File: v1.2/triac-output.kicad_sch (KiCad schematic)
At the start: 7 parts, among them Q5 T835-600B, Q6 2N7002, U7 TLP160G

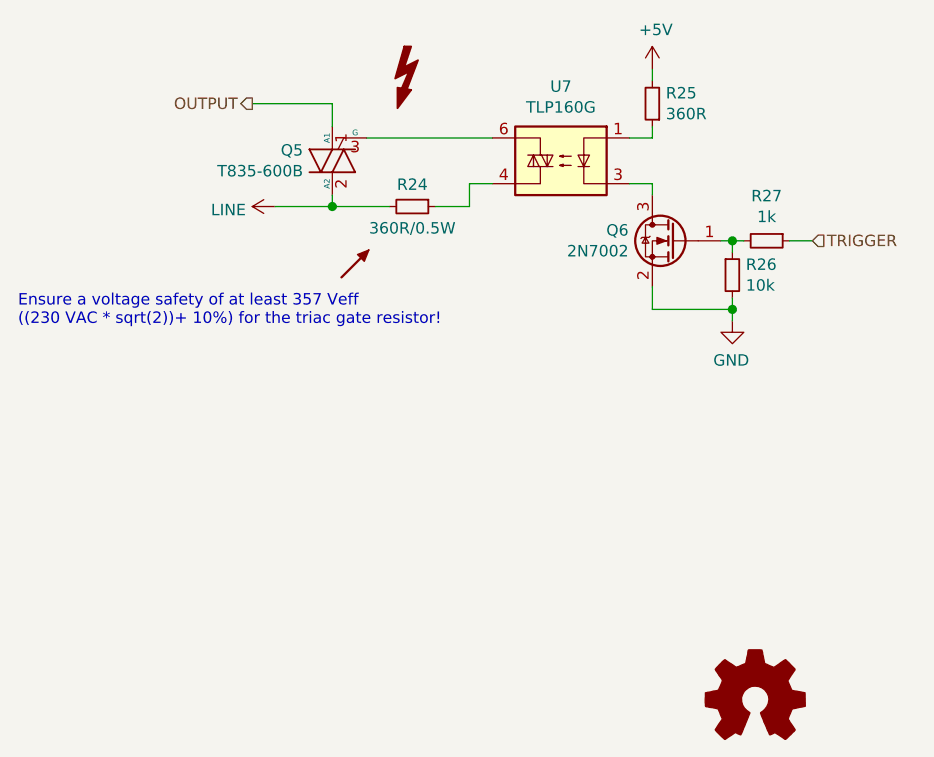
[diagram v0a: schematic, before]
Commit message: More updates
* make pump triac switch NEUT, not LINE
* move ADC a bit
* improve clearance
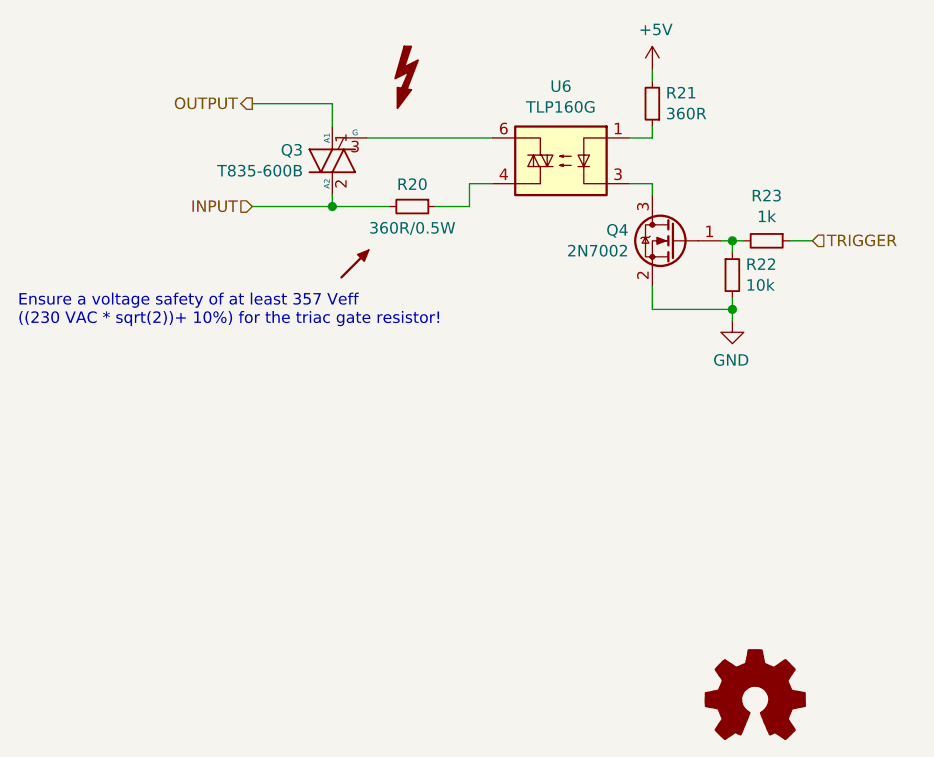
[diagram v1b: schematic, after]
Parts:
- renumbered Q5 to Q3, Q6 to Q4, R24 to R20, R25 to R21, R26 to R22, R27 to R23, U7 to U6
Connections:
- net LINE renamed INPUT
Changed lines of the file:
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@@
 (kicad_sch (version 20201015) (generator eeschema)
-  (page 0 6)
   (paper "A5")
   (title_block
@@
   (junction (at 133.35 60.96) (diameter 1.016) (color 0 0 0 0))
   (junction (at 133.35 68.58) (diameter 1.016) (color 0 0 0 0))
+  (wire (pts (xy 80.01 57.15) (xy 88.9 57.15))
+    (stroke (width 0) (type solid) (color 0 0 0 0))
+  )
   (wire (pts (xy 88.9 45.72) (xy 80.01 45.72))
     (stroke (width 0) (type solid) (color 0 0 0 0))
   )
   (wire (pts (xy 88.9 45.72) (xy 88.9 48.26))
-    (stroke (width 0) (type solid) (color 0 0 0 0))
-  )
-  (wire (pts (xy 88.9 57.15) (xy 82.55 57.15))
     (stroke (width 0) (type solid) (color 0 0 0 0))
   )
@@
     (effects (font (size 1.27 1.27)) (justify right))
   )
+  (hierarchical_label "INPUT" (shape input) (at 80.01 57.15 180)
+    (effects (font (size 1.27 1.27)) (justify right))
+  )
   (hierarchical_label "TRIGGER" (shape input) (at 142.24 60.96 0)
     (effects (font (size 1.27 1.27)) (justify left))
   )
-  (symbol (lib_id "power:LINE") (at 82.55 57.15 90) (mirror x)
-    (in_bom yes) (on_board yes)
-    (property "Reference" "#PWR048" (id 0) (at 86.36 57.15 0)
-      (effects (font (size 1.27 1.27)) hide)
-    )
-    (property "Value" "LINE" (id 1) (at 79.2988 57.531 90)
-      (effects (font (size 1.27 1.27)) (justify left))
-    )
-    (property "Footprint" "" (id 2) (at 82.55 57.15 0)
-      (effects (font (size 1.27 1.27)) hide)
-    )
-    (property "Datasheet" "" (id 3) (at 82.55 57.15 0)
-      (effects (font (size 1.27 1.27)) hide)
-    )
-  )
   (symbol (lib_id "power:+5V") (at 124.46 41.91 0)
     (in_bom yes) (on_board yes)
@@
   (symbol (lib_id "Device:R_Small") (at 97.79 57.15 270)
     (in_bom yes) (on_board yes)
-    (property "Reference" "R24" (id 0) (at 97.79 54.7116 90))
+    (property "Reference" "R20" (id 0) (at 97.79 54.7116 90))
     (property "Value" "360R/0.5W" (id 1) (at 97.79 59.563 90))
     (property "Footprint" "Resistor_SMD:R_1206_3216Metric_Pad1.30x1.75mm_HandSolder" (id 2) (at 97.79 57.15 0)
@@
   (symbol (lib_id "Device:R_Small") (at 124.46 45.72 180)
     (in_bom yes) (on_board yes)
-    (property "Reference" "R25" (id 0) (at 125.9586 44.5516 0)
+    (property "Reference" "R21" (id 0) (at 125.9586 44.5516 0)
       (effects (font (size 1.27 1.27)) (justify right))
     )
@@
   (symbol (lib_id "Device:R_Small") (at 133.35 64.77 0)
     (in_bom yes) (on_board yes)
-    (property "Reference" "R26" (id 0) (at 134.8486 63.6016 0)
+    (property "Reference" "R22" (id 0) (at 134.8486 63.6016 0)
       (effects (font (size 1.27 1.27)) (justify left))
     )
@@
   (symbol (lib_id "Device:R_Small") (at 137.16 60.96 270)
     (in_bom yes) (on_board yes)
-    (property "Reference" "R27" (id 0) (at 137.16 55.9816 90))
+    (property "Reference" "R23" (id 0) (at 137.16 55.9816 90))
     (property "Value" "1k" (id 1) (at 137.16 58.293 90))
     (property "Footprint" "Resistor_SMD:R_0603_1608Metric_Pad0.98x0.95mm_HandSolder" (id 2) (at 137.16 60.96 0)
@@
   (symbol (lib_id "Triac_Thyristor:BT138-600") (at 88.9 52.07 180)
     (in_bom yes) (on_board yes)
-    (property "Reference" "Q5" (id 0) (at 85.6488 50.9016 0)
+    (property "Reference" "Q3" (id 0) (at 85.6488 50.9016 0)
       (effects (font (size 1.27 1.27)) (justify left))
     )
@@
   (symbol (lib_id "Transistor_FET:2N7002") (at 127 60.96 0) (mirror y)
     (in_bom yes) (on_board yes)
-    (property "Reference" "Q6" (id 0) (at 121.8184 59.7916 0)
+    (property "Reference" "Q4" (id 0) (at 121.8184 59.7916 0)
       (effects (font (size 1.27 1.27)) (justify left))
     )
@@
   (symbol (lib_id "Relay_SolidState:TLP160G") (at 114.3 52.07 0) (mirror y)
     (in_bom yes) (on_board yes)
-    (property "Reference" "U7" (id 0) (at 114.3 43.815 0))
+    (property "Reference" "U6" (id 0) (at 114.3 43.815 0))
     (property "Value" "TLP160G" (id 1) (at 114.3 46.1264 0))
     (property "Footprint" "Package_SO:MFSOP6-4_4.4x3.6mm_P1.27mm" (id 2) (at 114.3 59.69 0)

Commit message: more cleanups, replace caps with ceramic types, polygon updates
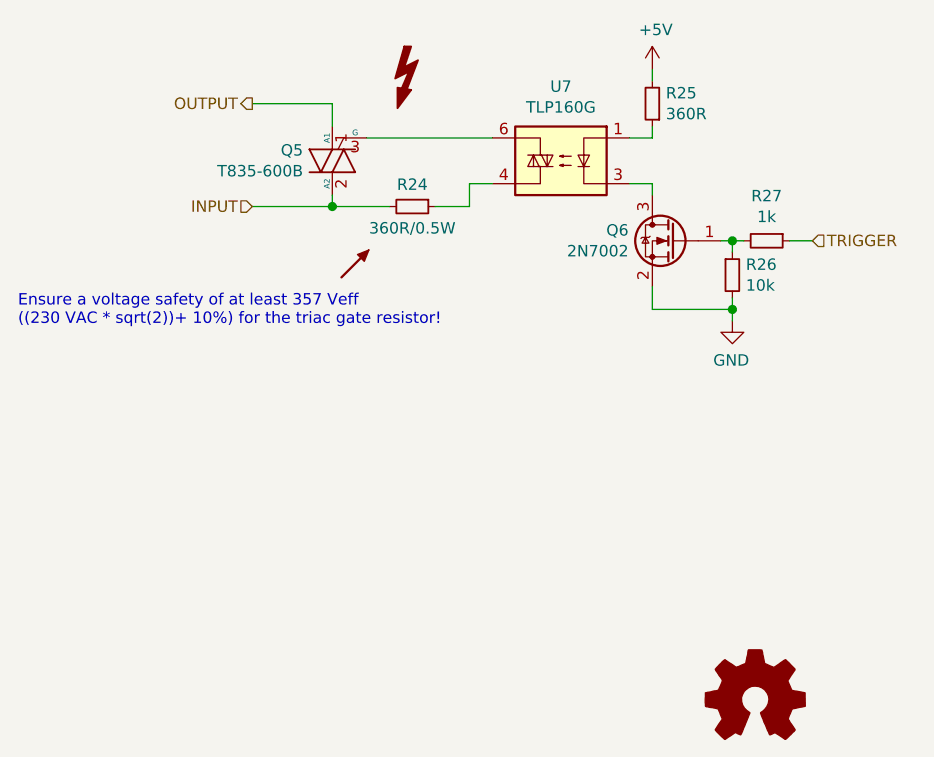
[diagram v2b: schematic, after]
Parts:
- renumbered Q3 to Q5, Q4 to Q6, R20 to R24, R21 to R25, R22 to R26, R23 to R27, U6 to U7
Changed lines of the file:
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@@
   (symbol (lib_id "Device:R_Small") (at 97.79 57.15 270)
     (in_bom yes) (on_board yes)
-    (property "Reference" "R20" (id 0) (at 97.79 54.7116 90))
+    (property "Reference" "R24" (id 0) (at 97.79 54.7116 90))
     (property "Value" "360R/0.5W" (id 1) (at 97.79 59.563 90))
     (property "Footprint" "Resistor_SMD:R_1206_3216Metric_Pad1.30x1.75mm_HandSolder" (id 2) (at 97.79 57.15 0)
@@
   (symbol (lib_id "Device:R_Small") (at 124.46 45.72 180)
     (in_bom yes) (on_board yes)
-    (property "Reference" "R21" (id 0) (at 125.9586 44.5516 0)
+    (property "Reference" "R25" (id 0) (at 125.9586 44.5516 0)
       (effects (font (size 1.27 1.27)) (justify right))
     )
@@
   (symbol (lib_id "Device:R_Small") (at 133.35 64.77 0)
     (in_bom yes) (on_board yes)
-    (property "Reference" "R22" (id 0) (at 134.8486 63.6016 0)
+    (property "Reference" "R26" (id 0) (at 134.8486 63.6016 0)
       (effects (font (size 1.27 1.27)) (justify left))
     )
@@
   (symbol (lib_id "Device:R_Small") (at 137.16 60.96 270)
     (in_bom yes) (on_board yes)
-    (property "Reference" "R23" (id 0) (at 137.16 55.9816 90))
+    (property "Reference" "R27" (id 0) (at 137.16 55.9816 90))
     (property "Value" "1k" (id 1) (at 137.16 58.293 90))
     (property "Footprint" "Resistor_SMD:R_0603_1608Metric_Pad0.98x0.95mm_HandSolder" (id 2) (at 137.16 60.96 0)
@@
   (symbol (lib_id "Triac_Thyristor:BT138-600") (at 88.9 52.07 180)
     (in_bom yes) (on_board yes)
-    (property "Reference" "Q3" (id 0) (at 85.6488 50.9016 0)
+    (property "Reference" "Q5" (id 0) (at 85.6488 50.9016 0)
       (effects (font (size 1.27 1.27)) (justify left))
     )
@@
   (symbol (lib_id "Transistor_FET:2N7002") (at 127 60.96 0) (mirror y)
     (in_bom yes) (on_board yes)
-    (property "Reference" "Q4" (id 0) (at 121.8184 59.7916 0)
+    (property "Reference" "Q6" (id 0) (at 121.8184 59.7916 0)
       (effects (font (size 1.27 1.27)) (justify left))
     )
@@
   (symbol (lib_id "Relay_SolidState:TLP160G") (at 114.3 52.07 0) (mirror y)
     (in_bom yes) (on_board yes)
-    (property "Reference" "U6" (id 0) (at 114.3 43.815 0))
+    (property "Reference" "U7" (id 0) (at 114.3 43.815 0))
     (property "Value" "TLP160G" (id 1) (at 114.3 46.1264 0))
     (property "Footprint" "Package_SO:MFSOP6-4_4.4x3.6mm_P1.27mm" (id 2) (at 114.3 59.69 0)
